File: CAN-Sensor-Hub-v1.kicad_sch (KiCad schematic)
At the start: 95 parts, among them J1 Conn_01x04, J10 Conn_01x03, J11 Conn_01x03, J12 Conn_01x12, J2 Conn_01x04, J3 Conn_01x04, J4 USB_C_Receptacle_USB2.0_14P, J5 Conn_ARM_JTAG_SWD_10, J6 Conn_01x02, J9 Conn_01x03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

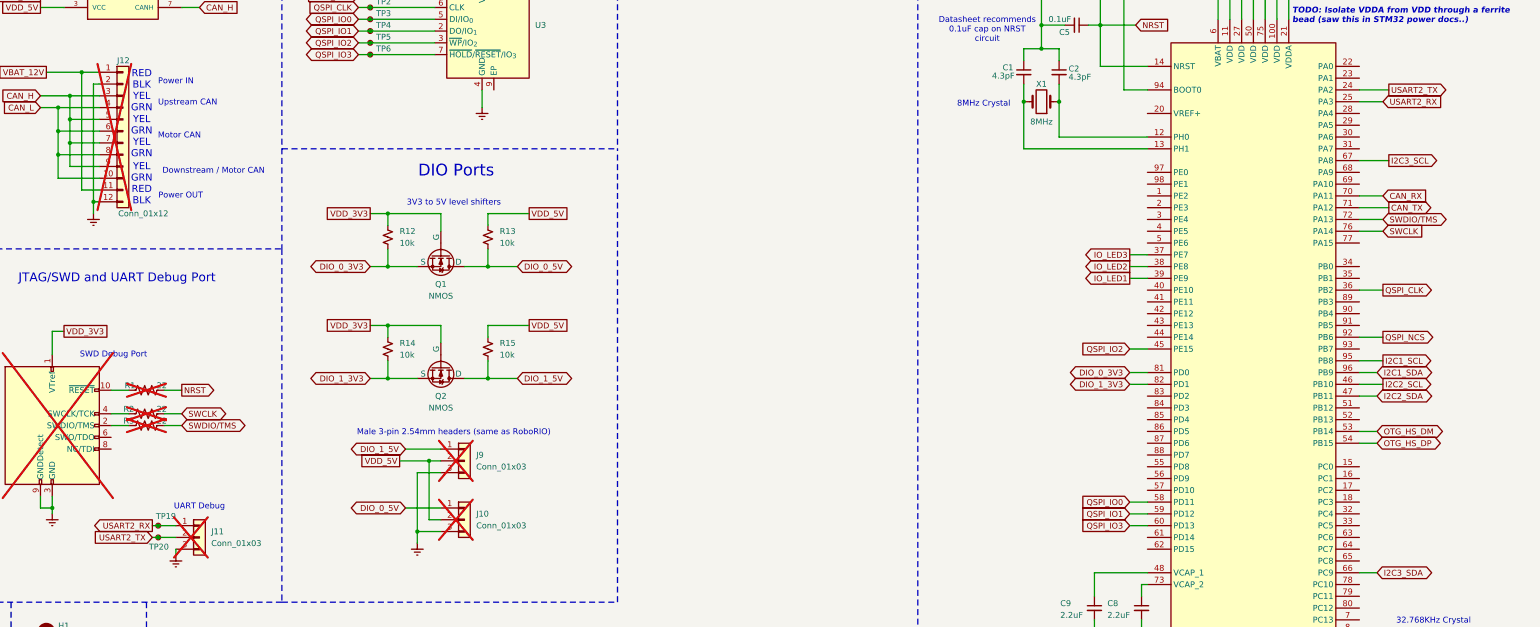
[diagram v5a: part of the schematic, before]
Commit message: Made some more adjustments .. USART2 is not compatible with bootloader, changed to USART1
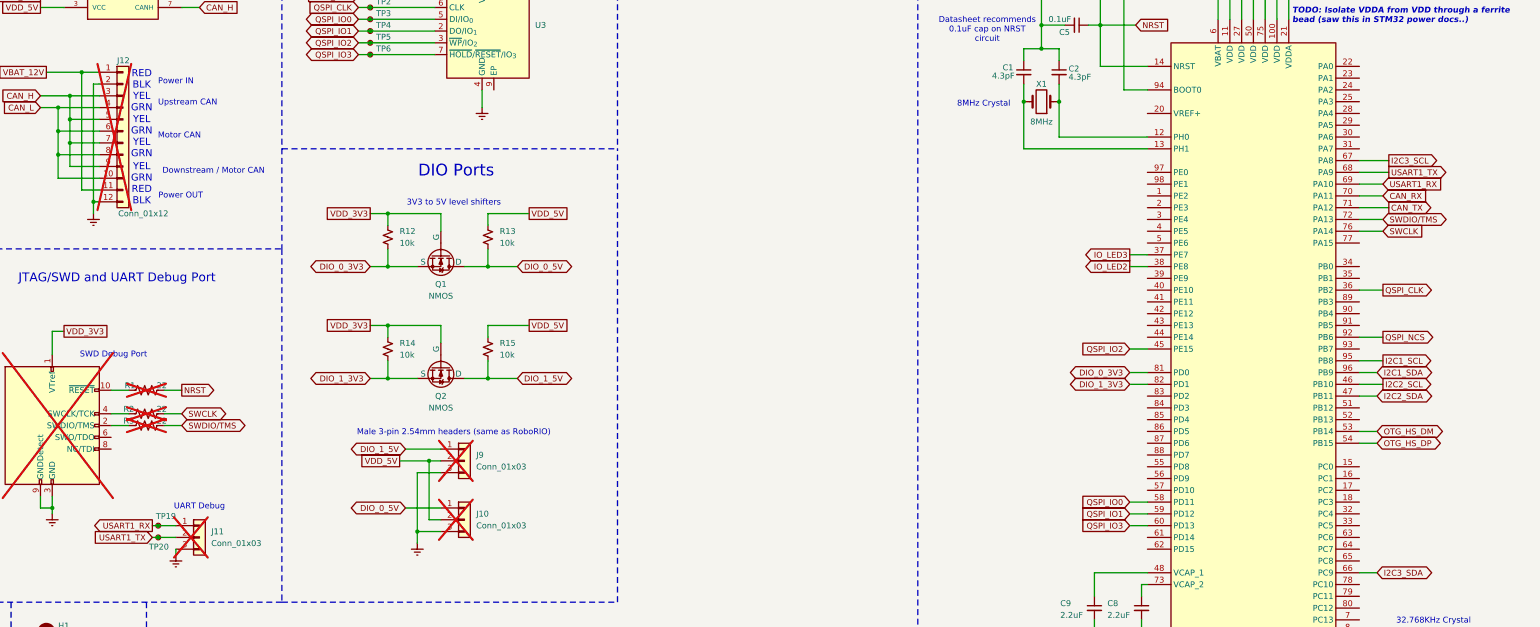
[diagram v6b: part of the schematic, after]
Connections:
- net USART1_TX: now reaches U7.68 (PA9)
- net USART1_TX: now also J11.2 (Pin_2), TP20.1
- net USART1_RX: now reaches U7.69 (PA10)
- net USART1_RX: now also J11.1 (Pin_1), TP19.1
- net IO_LED1: no longer names the net of U7.39 (PE9)
- removed net USART2_RX: J11.1 (Pin_1), TP19.1, U7.25 (PA3)
- removed net USART2_TX: J11.2 (Pin_2), TP20.1, U7.24 (PA2)
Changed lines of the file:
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@@
 	(wire
 		(pts
+			(xy 387.35 82.55) (xy 392.43 82.55)
+		)
+		(stroke
+			(width 0)
+			(type default)
+		)
+	)
+	(wire
+		(pts
 			(xy 118.11 210.82) (xy 118.11 215.9)
 		)
@@
 	(wire
 		(pts
-			(xy 337.82 102.87) (xy 341.63 102.87)
-		)
-		(stroke
-			(width 0)
-			(type default)
-		)
-	)
-	(wire
-		(pts
 			(xy 148.59 237.49) (xy 151.13 237.49)
 		)
@@
 	(wire
 		(pts
+			(xy 387.35 80.01) (xy 393.7 80.01)
+		)
+		(stroke
+			(width 0)
+			(type default)
+		)
+	)
+	(wire
+		(pts
 			(xy 24.13 180.34) (xy 24.13 182.88)
 		)
@@
 	(wire
 		(pts
-			(xy 387.35 62.23) (xy 393.7 62.23)
-		)
-		(stroke
-			(width 0)
-			(type default)
-		)
-	)
-	(wire
-		(pts
 			(xy 36.83 72.39) (xy 57.15 72.39)
 		)
@@
 	(wire
 		(pts
-			(xy 387.35 64.77) (xy 392.43 64.77)
-		)
-		(stroke
-			(width 0)
-			(type default)
-		)
-	)
-	(wire
-		(pts
 			(xy 330.2 171.45) (xy 330.2 166.37)
 		)
@@
 			"AAAAAAAAAAAAAAAAEhoAAAAcAgAAAAAAAAAAAAADAACEAgAAAAAAAAAAAADgojOmBwAAAAAAAAAA"
 			"AAAAAAAAAAAAAABNEwAAABwCAAAAAAAAAAAAhQIAAF4CAAAAAAAAAAAAAMCPyXQHAAAAAAAAAAAA"
-			"AAAAAAAAAAAAAMgGAAAAHAIAAAAAAAAAAABxBAAAdAIAAAAAAAAAAAAAENqIpgcAAAAAAA=="
+			"AAAAAAAAAAAAAMgGAAAAHAIAAAAAAAAAAABxBAAAdAIAAAAAAAAAAAAAENqIpgcAAAAAAAAAAAAA"
+			"AAAAAAAAAAAAAAAAAAAAAAAAAAAAAAAAAAAAAAAAAAAAAAAAAAAAAAAAAAAAAAAAAAAAAAAAAAAA"
+			"AAAAAAAAAAAAAAAAAAAAAAAAAAAAAAAAAAAAAAAAAAAAAAAAAAAAAAAAAAAAAAAAAAAAAAAAAAAA"
+			"AAAAAAAAAAAAAAAAAAAAAAAAAAAAAAAAAAAAAAAAAAAAAAAAAAAAAAAAAAAAAAAAAAAAAAAAAAAA"
+			"AAAAAAAAAAAAAAAAAAAAAAAAAAAAAAAAAAAAAAAAAAAAAAAAAAAAAAAAAAAAAAAAAAAAAAAAAAAA"
+			"AAAAAAAAAAAAAAAAAAAAAAAAAAAAAAAAAAAAAAAAAAAAAAAAAAAAAAAAAAAAAAAAAAAAAAAAAAAA"
+			"AAAAAAAAAAAAAAAAAAAAAAAAAAAAAAAAAAAAAAAAAAAAAAAAAAAAAAAAAAAAAAAAAAAAAAAAAAAA"
+			"AAAAAAAAAAAAAAAAAAAAAAAAAAAAAAAAAAAAAAAAAAAAAAAAAAAAAAAAAAAAAAAAAAAAAAAAAAAA"
+			"AAAAAAAAAAAAAAAAAAAAAAAAAAAAAAAAAAAAAAAAAAAAAAAAAAAAAAAAAAAAAAAAAAAAAAAAAAAA"
+			"AAAAAAAAAAAAAAAAAAAAAAAAAAAAAAAAAAAAAAAAAAAAAAAAAAAAAAAAAAAAAAAAAAAAAAAAAAAA"
+			"AAAAAAAAAAAAAAAAAAAAAAAAAAAAAAAAAAAAAAAAAAAAAAAAAAAAAAAAAAAAAAAAAAAAAAAAAAAA"
+			"AAAAAAAAAAAAAAAAAAAAAAAAAAAAAAAAAAAAAAAAAAAAAAAAAAAAAAAAAAAAAAAAAAAAAAAAAAAA"
+			"AAAAAAAAAAAAAAAAAAAAAAAAAAAAAAAAAAAAAAAAAAAAAAAAAAAAAAAAAAAAAAAAAAAAAAAAAAAA"
+			"AAAAAAAAAAAAAAAAAAAAAAAAAAAAAAAAAAAAAAAAAAAAAAAAAAAAAAAAAAAAAAAAAAAAAAAAAAAA"
+			"AAAAAAAAAAAAAAAAAAAAAAAAAAAAAAAAAAAAAAAAAAAAAAAAAAAAAAAAAAAAAAAAAAAAAAAAAAAA"
+			"AAAAAAAAAAAAAAAAAAAAAAAAAAAAAAAAAAAAAAAAAAAAAAAAAAAAAAAAAAAAAAAAAAAAAAAAAAAA"
+			"AAAAAAAAAAAAAAAAAAAAAAAAAAAAAAAAAAAAAAAAAAAAAAAAAAAAAAAAAAAAAAAAAAAAAAAAAAAA"
+			"AAAAAAAAAAAAAAAAAAAAAAAAAAAAAAAAAAAAAAAAAAAAAAAAAAAAAAAAAAAAAAAAAAAAAAAAAAAA"
+			"AAAAAAAAAAAAAAAAAAAAAAAAAAAAAAAAAAAAAAAAAAAAAAAAAAAAAAAAAAAAAAAAAAAAAIguiC6I"
+			"LoguiC6ILoguiC6ILoguiC6ILoguiC6ILoguiC6ILoguiC6ILoguiC6ILoguiC6ILoguiC6ILogu"
+			"iC6ILoguiC6ILoguiC6ILoguiC6ILoguiC6ILoguiC6ILoguiC6ILoguiC6ILoguiC6ILoguiC6I"
+			"LoguiC6ILoguiC6ILoguiC6ILoguiC6ILoguiC6ILoguiC6ILoguiC6ILoguiC6ILoguiC6ILogu"
+			"iC6ILoguiC6ILoguiC6ILoguiC6ILoguiC6ILoguiC6ILoguiC6ILoguiC6ILoguiC6ILoguiC6I"
+			"LoguiC6ILoguiC6ILoguiC6ILoguiC6ILoguiC6ILoguiC6ILoguiC6ILoguiC6ILoguiC6ILogu"
+			"iC6ILoguiC6ILoguiC6ILoguiC6ILoguiC6ILoguiC6ILoguiC6ILoguiC6ILoguiC6ILoguiC6I"
+			"LoguiC6ILoguiC6ILoguiC6ILoguiC6ILoguiC6ILoguiC6ILoguiC6ILoguiC6ILoguiC6ILogu"
+			"iC6ILoguiC6ILoguiC6ILoguiC6ILoguiC6ILoguiC6ILoguiC6ILoguiC6ILoguiC6ILoguiC6I"
+			"LoguiC6ILoguiC6ILoguiC6ILoguiC6ILoguiC6ILoguiC6ILoguiC6ILoguiC6ILoguiC6ILogu"
+			"iC6ILoguiC6ILoguiC6ILoguiC6ILoguiC6ILoguiC6ILoguiC6ILoguiC6ILoguiC6ILoguiC6I"
+			"LoguiC6ILoguiC6ILoguiC6ILoguiC6ILoguiC6ILoguiC6ILoguiC6ILoguiC6ILoguiC6ILogu"
+			"iC6ILoguiC6ILoguiC6ILoguiC6ILoguiC6ILoguiC6ILoguiC6ILoguiC6ILoguiC6ILoguiC6I"
+			"LoguiC6ILoguiC6ILoguiC6ILoguiC6ILoguiC6ILoguiC6ILoguiC6ILoguiC6ILoguiC6ILogu"
+			"iC6ILoguiC6ILoguiC6ILoguiC6ILoguiC6ILoguiC6ILoguiC6ILoguiC6ILoguiC6ILoguiC6I"
+			"LoguiC6ILoguiC6ILoguiC6ILoguiC6ILoguiC6ILoguiC6ILoguiC6ILoguiC6ILoguiC6ILogu"
+			"iC6ILoguiC6ILoguiC6ILoguiC6ILoguiC6ILoguiC6ILoguiC6ILoguiC6ILoguiC6ILoguiC6I"
+			"LoguiC6ILoguiC6ILoguiC6ILoguiC6ILoguiC6ILoguiC6ILoguiC6ILoguiC6ILoguiC6ILogu"
+			"iC6ILoguiC6ILoguiC6ILoguiC6ILoguiC6ILoguiC6ILoguiC6ILoguiC6ILoguiC6ILg=="
 		)
 	)
@@
 			"x//j4uH/AAAAAAAAAACrPhvAhEIAwNF5TT4AAH9/0tHH/+Pi4f8AAAAAAAAAACHIGcBFZPi/0XlN"
 			"PgAAf3/S0cf/4+Lh/wAAAAAAAAAAvysewHGsA8DReU0+AAB/f9LRx//j4uH/AAAAAAAAAAAhyBnA"
-			"RWT4v9F5TT4AAH9/0tHH/+Pi4f8AAA=="
+			"RWT4v9F5TT4AAH9/0tHH/+Pi4f8AAAAAAAAAAAAAAAAAAAAAbPfCHAAAAAAAeflWBwAAAAB5+VYH"
+			"AAAAbffCHAAAAAAAevlWBwAAAAB6+VYHAAAAbvfCHAAAAAAAe/lWBwAAAAB7+VYHAAAAzBcCAAAA"
+			"AACAaPlWBwAAAIBo+VYHAAAAAQAAgAAAAAAAAAAAAAAAAAAAAAAAAAAAcffCHAAAAAAAfPlWBwAA"
+			"AAB8+VYHAAAAcvfCHAAAAAAAfvlWBwAAAAB++VYHAAAAAQAAgAAAAAAAAAAAAAAAAAAAAAAAAAAA"
+			"0NI8egAAAACAsgpZBwAAAICyClkHAAAAAQAAgAAAAAAAAAAAAAAAAAAAAAAAAAAArEsCAAAAAAAA"
+			"zwpZBwAAAADPClkHAAAAAQAAgAAAAAAAAAAAAAAAAAAAAAAAAAAAAQAAgAAAAAAAAAAAAAAAAAAA"
+			"AAAAAAAAAQAAgAAAAAAAAAAAAAAAAAAAAAAAAAAAAQAAgAAAAAAAAAAAAAAAAAAAAAAAAAAAAQAA"
+			"gAAAAAAAAAAAAAAAAAAAAAAAAAAAAQAAgAAAAAAAAAAAAAAAAAAAAAAAAAAAAQAAgAAAAAAAAAAA"
+			"AAAAAAAAAAAAAAAA0/fCHAAAAACAkQpZBwAAAICRClkHAAAA5BnFHAAAAACAngpZBwAAAICeClkH"
+			"AAAAq0XzIwAAAACAzLhWBwAAAIDMuFYHAAAAAQAAgAAAAAAAAAAAAAAAAAAAAAAAAAAAAQAAgAAA"
+			"AAAAAAAAAAAAAAAAAAAAAAAAykHFHAAAAACAEgtZBwAAAIASC1kHAAAAAQAAgAAAAAAAAAAAAAAA"
+			"AAAAAAAAAAAAhffCHAAAAACACOpWBwAAAIAI6lYHAAAAAQAAgAAAAAAAAAAAAAAAAAAAAAAAAAAA"
+			"AQAAgAAAAAAAAAAAAAAAAAAAAAAAAAAAAQAAgAAAAAAAAAAAAAAAAAAAAAAAAAAAiffCHAAAAAAA"
+			"FOpWBwAAAAAU6lYHAAAAqeRAVgAAAAAANgtZBwAAAAA2C1kHAAAAAQAAgAAAAAAAAAAAAAAAAAAA"
+			"AAAAAAAAAQAAgAAAAAAAAAAAAAAAAAAAAAAAAAAAAQAAgAAAAAAAAAAAAAAAAAAAAAAAAAAAAQAA"
+			"gAAAAAAAAAAAAAAAAAAAAAAAAAAAAQAAgAAAAAAAAAAAAAAAAAAAAAAAAAAAAQAAgAAAAAAAAAAA"
+			"AAAAAAAAAAAAAAAAsmcCAAAAAAAALwtZBwAAAAAvC1kHAAAA10XFHAAAAACAHgtZBwAAAIAeC1kH"
+			"AAAAk/fCHAAAAACAgQpZBwAAAICBClkHAAAAAQAAgAAAAAAAAAAAAAAAAAAAAAAAAAAAAQAAgAAA"
+			"AAAAAAAAAAAAAAAAAAAAAAAAAQAAgAAAAAAAAAAAAAAAAAAAAAAAAAAAAAAAAAAAAAAAAAAAAAAA"
+			"AAAAAAAAAAAAAAAAAAAAAAAAAAAAAAAAAAAAAAAAAAAAAAAAAAAAAAAAAAAAAAAAAAAAAAAAAAAA"
+			"AAAAAAAAAAAAAAAAAAAAAAAAAAAAAAAAAAAAAAAAAAAAAAAAAAAAAAAAAAAAAAAAAAAAAAAAAAAA"
+			"AAAAAAAAAAAAAAAAAAAAAAAAAAAAAAAAAAAAAAAAAAAAAAAAAAAAAAAAAAAAAAAAAAAAAAAAAAAA"
+			"AAAAAAAAAAAAAAAAAAAAAAAAAAAAAAAAAAAAAAAAAAAAAAAAAAAAAAAAAAAAAAAAAAAAAAAAAAAA"
+			"AAAAAAAAAAAAAAAAAAAAAAAAAAAAAAAAAAAAAAAAAAAAAAAAAAAAAAAAAAAAAAAAAAAAAAAAAAAA"
+			"AAAAAAAAAAAAAAAAAAAAAAAAAAAAAAAAAAAAAAAAAAAAAAAAAAAAAAAAAAAAAAAAAAAAAAAAAAAA"
+			"AAAAAAAAAAAAAAAAAAAAAAAAAAAAAAAAAAAAAAAAAAAAAAAAAAAAAAAAAAAAAAAAAAAAAAAAAAAA"
+			"AAAAAAAAAAAAAAAAAAAAAAAAAAAAAAAAAAAAAAAAAAAAAAAAAAAAAAAAAAAAAAAAAAAAAAAAAAAA"
+			"AAAAAAAAAAAAAAAAAAAAAAAAAAAAAAAAAAAAAAAAAAAAAAAAAAAAAAAAAAAAAAAAAAAAAAAAAAAA"
+			"AAAAAAAAAAAAAAAAAAAAAAAAAAAAAAAAAAAAAAAAAAAAAAAAAAAAAAAAAAAAAAAAAAAAAAAAAAAA"
+			"AAAAAAAAAAAAAAAAAAAAAAAAAAAAAAAAAAAAAAAAAAAAAAAAAAAAAAAAAAAAAAAAAAAAAAAAAAAA"
+			"AAAAAAAAAAAAAAAAAAAAAAAAAAAAAAAAAAAAAAAAAAAAAAAAAAAAAAAAAAAAAAAAAAAAAAAAAAAA"
+			"AAAAAAAAAAAAAAAAAAAAAAAAAAAAAAAAAAAAAAAAAAAAAAAAAAAAAAAAAAAAAAAAAAAAAAAAAAAA"
+			"AAAAAAAAAAAAAAAAAAAAAAAAAAAAAAAAAAAAAAAAAAAAAAAAAAAAAAAAAAAAAAAAAAAAAAAAAAAA"
+			"AAAAAAAAAAAAAAAAAAAAAAAAAAAAAAAAAAAAAAAAAAAAAAAAAAAAAAAAAAAAAAAAAAAAAAAAAAAA"
+			"AAAAAAAAAAAAAAAAAAAAAAAAAAAAAAAAAAAAAAAAAAAAAAAAAAAAAAAAAAAAAAAAAAAAAAAAAAAA"
+			"AAAAAAAAAAAAAAAAAAAAAAAAAAAAAAAAAAAAAAAAAAAAAAAAAAAAAAAAAAAAAAAAAAAAAAAAAAAA"
+			"AAAAAAAAAAAAAAAAAAAAAAAAAAAAAA=="
 		)
 	)
@@
 		)
 	)
-	(global_label "USART2_RX"
+	(global_label "USART1_RX"
 		(shape output)
 		(at 127 156.21 180)
@@
 		)
 	)
-	(global_label "USART2_TX"
+	(global_label "USART1_TX"
 		(shape input)
 		(at 127 158.75 180)
@@
 		)
 	)
-	(global_label "IO_LED1"
-		(shape output)
-		(at 337.82 102.87 180)
-		(fields_autoplaced yes)
-		(effects
-			(font
-				(size 1.27 1.27)
-			)
-			(justify right)
-		)
-		(property "Intersheetrefs" "${INTERSHEET_REFS}"
-			(at 327.2753 102.87 0)
-			(effects
-				(font
-					(size 1.27 1.27)
-				)
-				(justify right)
-				(hide yes)
-			)
-		)
-	)
 	(global_label "VDD_5V"
 		(shape passive)
@@
 		)
 	)
-	(global_label "USART2_TX"
+	(global_label "USART1_TX"
 		(shape output)
-		(at 393.7 62.23 0)
+		(at 393.7 80.01 0)
 		(fields_autoplaced yes)
 		(effects
@@
 		)
 		(property "Intersheetrefs" "${INTERSHEET_REFS}"
-			(at 406.9056 62.23 0)
+			(at 406.9056 80.01 0)
 			(effects
 				(font
@@
 		)
 	)
-	(global_label "USART2_RX"
+	(global_label "USART1_RX"
 		(shape input)
-		(at 392.43 64.77 0)
+		(at 392.43 82.55 0)
 		(fields_autoplaced yes)
 		(effects
@@
 		)
 		(property "Intersheetrefs" "${INTERSHEET_REFS}"
-			(at 405.938 64.77 0)
+			(at 405.938 82.55 0)
 			(effects
 				(font
